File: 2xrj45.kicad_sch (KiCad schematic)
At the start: 6 parts, among them J1 Bus_RJ45_7499111121A, J2 Bus_RJ45_7499111121A

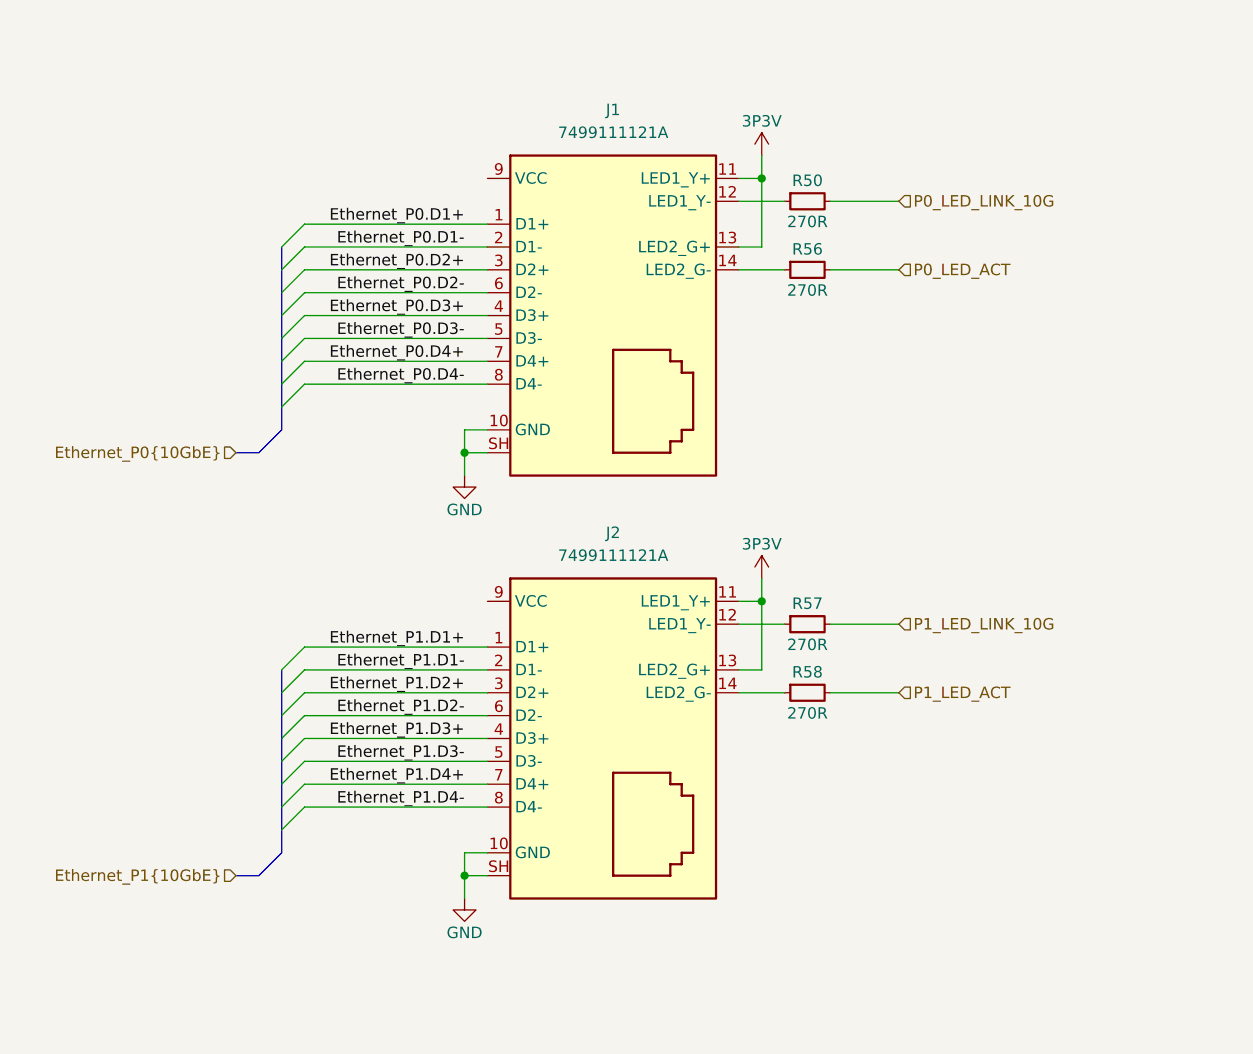
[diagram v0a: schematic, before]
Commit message: [#80813] Change RJ45 connectors, reannotate schematics
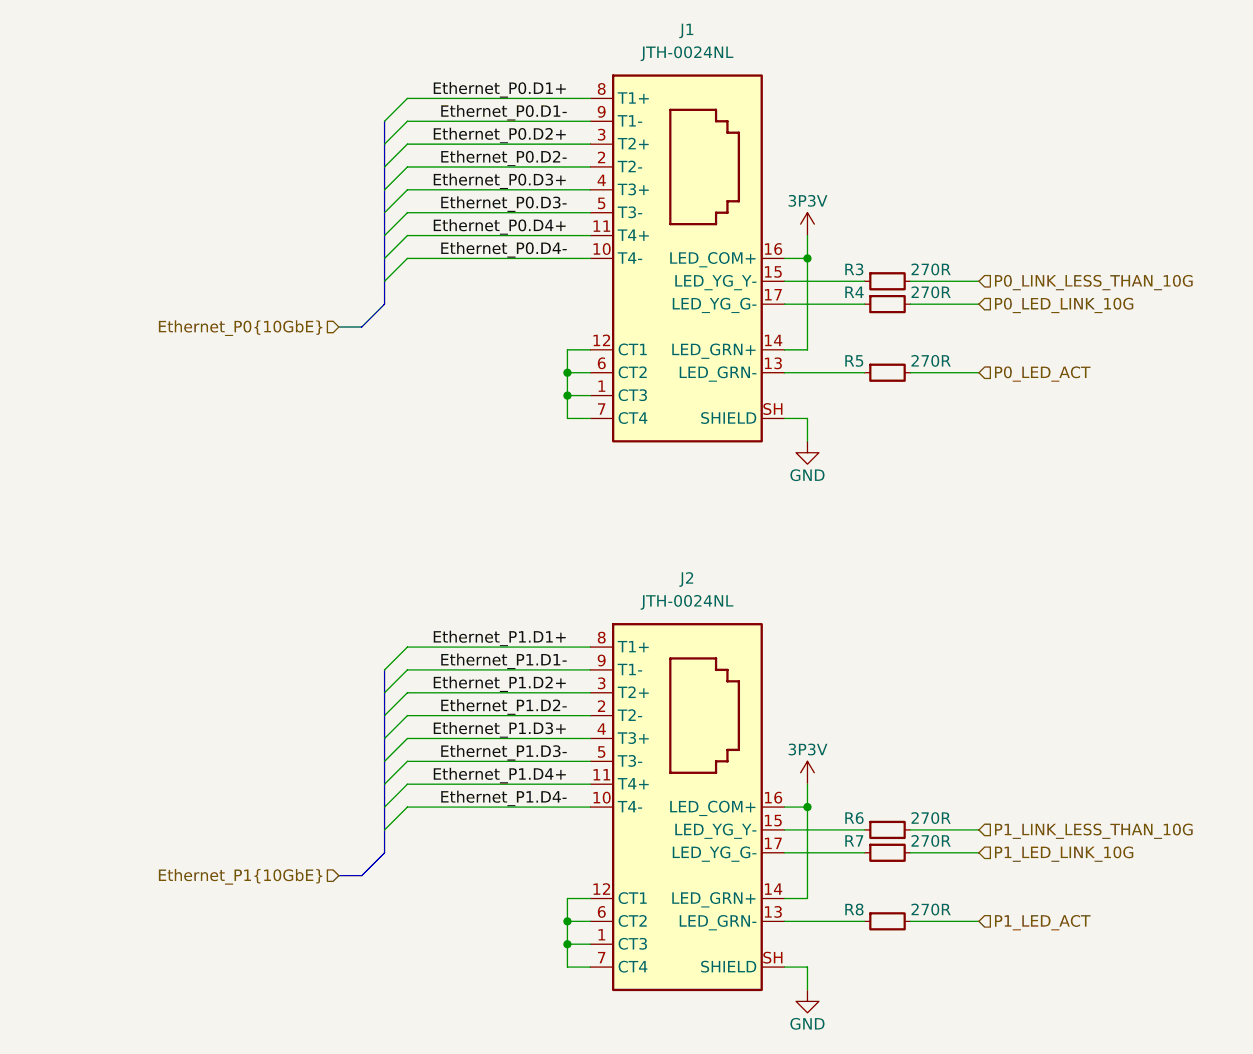
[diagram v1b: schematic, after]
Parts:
- removed J1, J2: Bus_RJ45_7499111121A, antmicro-footprints:RJ45_7499111121A_Horizontal, symbol antmicroModularConnectorsJacksWithMagnetics:Bus_RJ45_7499111121A
- removed R56, R57, R58: R_270R_0402, antmicro-footprints:R_0402_1005Metric, symbol antmicroResistors0402:R_270R_0402
- added J1, J2: Bus_RJ45_JTH-0024NL, antmicro-footprints:RJ45_JTH-0024NL, symbol antmicroModularConnectorsJacksWithMagnetics:Bus_RJ45_JTH-0024NL
- added R4, R5, R6, R7, R8: R_270R_0402, antmicro-footprints:R_0402_1005Metric, symbol antmicroResistors0402:R_270R_0402
- renumbered R50 to R3
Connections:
- net 3P3V: now also J1.14 (LED_GRN+), J1.16 (LED_COM+), J2.14 (LED_GRN+), J2.16 (LED_COM+)
- net Ethernet_P0.D1+: now also J1.8 (T1+)
- net Ethernet_P0.D1-: now also J1.9 (T1-)
- net Ethernet_P0.D2+: now also J1.3 (T2+)
- net Ethernet_P0.D2-: now also J1.2 (T2-)
- net Ethernet_P0.D3+: now also J1.4 (T3+)
- net Ethernet_P0.D3-: now also J1.5 (T3-)
- net Ethernet_P0.D4+: now also J1.11 (T4+)
- net Ethernet_P0.D4-: now also J1.10 (T4-)
- net Ethernet_P1.D1+: now also J2.8 (T1+)
- net Ethernet_P1.D1-: now also J2.9 (T1-)
- net Ethernet_P1.D2+: now also J2.3 (T2+)
- net Ethernet_P1.D2-: now also J2.2 (T2-)
- net Ethernet_P1.D3+: now also J2.4 (T3+)
- net Ethernet_P1.D3-: now also J2.5 (T3-)
- net Ethernet_P1.D4+: now also J2.11 (T4+)
- net Ethernet_P1.D4-: now also J2.10 (T4-)
- net GND: now also J1.SH (SHIELD), J2.SH (SHIELD)
- net P0_LED_ACT: now also R5.2
- net P0_LED_LINK_10G: now also R4.2; no longer R3.2
- net P1_LED_ACT: now also R8.2
- net P1_LED_LINK_10G: now also R7.2
- net at R3.1: now also J1.15 (LED_YG_Y-)
- new net: J2.1 (CT3), J2.12 (CT1), J2.6 (CT2), J2.7 (CT4)
- new net: J2.13 (LED_GRN-), R8.1
- new net: J2.15 (LED_YG_Y-), R6.1
- new net: J2.17 (LED_YG_G-), R7.1
- new net: J1.17 (LED_YG_G-), R4.1
- new net: J1.1 (CT3), J1.12 (CT1), J1.6 (CT2), J1.7 (CT4)
- new net: J1.13 (LED_GRN-), R5.1
- new net P0_LINK_LESS_THAN_10G: R3.2
- new net P1_LINK_LESS_THAN_10G: R6.2
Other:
- moved on the sheet: R3

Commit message: [#80813] Improve schematic readability, add debug connectors and missing resistors
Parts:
- added C24, C25, C26, C27, C28, C29, C30, C31, C32: C_1u_25V_0402, antmicro-footprints:C_0402_1005Metric, symbol antmicroCapacitors0402:C_1u_25V_0402
- added C33: C_22u_16V_0603, antmicro-footprints:C_0603_1608Metric_EIA, symbol antmicroCapacitors0603:C_22u_16V_0603
- added FB2: FB_120Z_1.2A_TDK-MPZ_0402, antmicro-footprints:FB_0402_1005Metric, symbol antmicroFerriteBeadsandChips:FB_120Z_1.2A_TDK-MPZ_0402
- added L2: L_2n4_0.85A_0402, antmicro-footprints:L_0402_1005Metric, symbol antmicroFixedInductors:L_2n4_0.85A_0402
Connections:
- net Ethernet_P0.D1+: now also J1.11 (T4+); no longer J1.8 (T1+)
- net Ethernet_P0.D1-: now also J1.10 (T4-); no longer J1.9 (T1-)
- net Ethernet_P0.D2+: now also J1.4 (T3+); no longer J1.3 (T2+)
- net Ethernet_P0.D2-: now also J1.5 (T3-); no longer J1.2 (T2-)
- net Ethernet_P0.D3+: now also J1.3 (T2+); no longer J1.4 (T3+)
- net Ethernet_P0.D3-: now also J1.2 (T2-); no longer J1.5 (T3-)
- net Ethernet_P0.D4+: now also J1.8 (T1+); no longer J1.11 (T4+)
- net Ethernet_P0.D4-: now also J1.9 (T1-); no longer J1.10 (T4-)
- net GND: now also C24.1, C25.1, C26.1, C27.1, C28.1, C29.1, C30.1, C31.1
- net at J2.1 (CT3), J2.12 (CT1), J2.6 (CT2)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: now also C28.2, C29.2, C30.2, C31.2
- net at J1.1 (CT3), J1.12 (CT1), J1.6 (CT2)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: now also C24.2, C25.2, C26.2, C27.2, L2.2
- net P0_LED_ACT renamed ~{P0_LED_ACT}
- net P0_LED_LINK_10G renamed ~{P0_LED_LINK_10G}
- net P0_LINK_LESS_THAN_10G renamed ~{P0_LINK_LESS_THAN_10G}
- net P1_LED_ACT renamed ~{P1_LED_ACT}
- net P1_LED_LINK_10G renamed ~{P1_LED_LINK_10G}
- net P1_LINK_LESS_THAN_10G renamed ~{P1_LINK_LESS_THAN_10G}
- new net: C32.2, FB2.2
- new net: C33.2, FB2.1
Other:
- note added: "10GbE Port 0"
- note added: "10GbE Port 1"
- moved on the sheet: J1, J2, R3, R4, R5, R6, R7, R8
